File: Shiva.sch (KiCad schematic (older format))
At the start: 6 parts

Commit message: Add 8 input channels, Teensy, start MIDI interface
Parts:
- added BOARD?: BOARD_TEENSY_3.1, symbol BOARD_TEENSY_3.1
- added D? (x7): 3.3, symbol ZENER
- added D? (x7): 3.3V, symbol ZENER
- added D?: D, symbol D
- added J? (x7): JACK_FEMALE_STEREO, symbol CONNECTORS_JACK_FEMALE_STEREO_6_PINS
- added JP? (x8): Jumper_NO_Small, symbol Jumper_NO_Small
- added P? (x2): DIN_5, symbol DIN_5
- added R? (x7): 320M, symbol R
- added R? (x18): R, symbol R
- added U? (x8): LTC6242, symbol ANALOG_LTC6242
- D?: value ZENER -> 3.3
- D?: value ZENER -> 3.3V
- R?: value R -> 320M
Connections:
- net labels added: CHANNEL_01, CHANNEL_02, CHANNEL_03, CHANNEL_04, CHANNEL_05, CHANNEL_06, CHANNEL_07, CHANNEL_08, DETECT_02, DETECT_03, DETECT_04, DETECT_05, DETECT_06, DETECT_07, DETECT_08
- wire segments 18 -> 200
- no-connect marks 3 -> 24
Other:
- note added: "Features remaining:\n- MIDI OUT\n- MIDI IN ?\n- Regulator"
- moved on the sheet: D?, J?, R?

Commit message: Add MIDI and regulator
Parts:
- removed D?: D, symbol D
- removed P?: DIN_5, symbol DIN_5
- removed R? (x2): R, symbol R
- added C1, C2, C3: 100nF, symbol C
- added C4: 10uF, symbol C
- added JP10, JP9: Jumper_NO_Small, symbol Jumper_NO_Small
- added U3: LD1117S33CTR, SOT-223, symbol LD1117S33CTR
- R25, R26: renamed from R?; value R -> 220R
- gave numbers to parts that had none: 60
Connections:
- net CHANNEL_01: now also U1.16 (OUT); no longer U1.1 (OUT)
- net CHANNEL_04: now also U1.1 (OUT); no longer U1.16 (OUT)
- net CHANNEL_05: now also U2.16 (OUT); no longer U2.1 (OUT)
- net CHANNEL_06: now also U2.7 (OUT); no longer U2.1 (OUT)
- net CHANNEL_07: now also U2.10 (OUT); no longer U2.1 (OUT)
- net GND: now also BOARD1.1 (GND), P1.2; no longer U1.13 (V-), U1.13 (V-), U1.13 (V-), U1.13 (V-), U2.13 (V-), U2.13 (V-), U2.13 (V-), U2.13 (V-)
- net VCC: now also C1.1, C2.1, JP10.2, JP9.2
- net at D7.2 (A), D8.1 (K), J4.T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: now also U1.15 (-IN); no longer U1.2 (-IN)
- net at R12.2, R8.1: now also U1.14 (+IN); no longer U1.3 (+IN)
- net at D1.2 (A), D2.1 (K), J1.T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: now also U1.2 (-IN); no longer U1.15 (-IN)
- net at R5.1, R9.2: now also U1.3 (+IN); no longer U1.14 (+IN)
- net at D15.2 (A), D16.1 (K), J8.T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: now also U2.15 (-IN); no longer U2.2 (-IN)
- net at R20.1, R24.2: now also U2.14 (+IN); no longer U2.3 (+IN)
- net at D11.2 (A), D12.1 (K), J6.T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: now also U2.6 (-IN); no longer U2.2 (-IN)
- net at R18.1, R22.2: now also U2.5 (+IN); no longer U2.3 (+IN)
- net at D13.2 (A), D14.1 (K), J7.T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: now also U2.11 (-IN); no longer U2.2 (-IN)
- net at R19.1, R23.2: now also U2.12 (+IN); no longer U2.3 (+IN)
- net RX: now reaches BOARD1.2 (D0/RX1)
- net RX: now also R26.1
- net GNDA: now reaches BOARD1.27 (AGND)
- net GNDA: now also U1.13 (V-), U1.13 (V-), U1.13 (V-), U1.13 (V-), U2.13 (V-), U2.13 (V-), U2.13 (V-), U2.13 (V-), C1.2, C2.2, C3.2, C4.2, U3.1 (GND)
- net +5V: now reaches BOARD1.28 (Vin)
- net +5V: now also R25.1, C3.1, JP9.1, U3.3 (VI)
- net at P1.4: now also R26.2
- net at P1.5: now also R25.2
- new net: C4.1, JP10.1, U3.2 (VO)
- no-connect marks 24 -> 34
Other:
- note added: "(As close as possible \nto op-amp IC)"
- note added: "MIDI OUT"
- note added: "Select source at \nassembly"
- note removed: "Features remaining:\n- MIDI OUT\n- MIDI IN ?\n- Regulator"
- moved on the sheet: D1, D10, D11, D12, D13, D14, D15, D16, D2, D3, D4, D5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

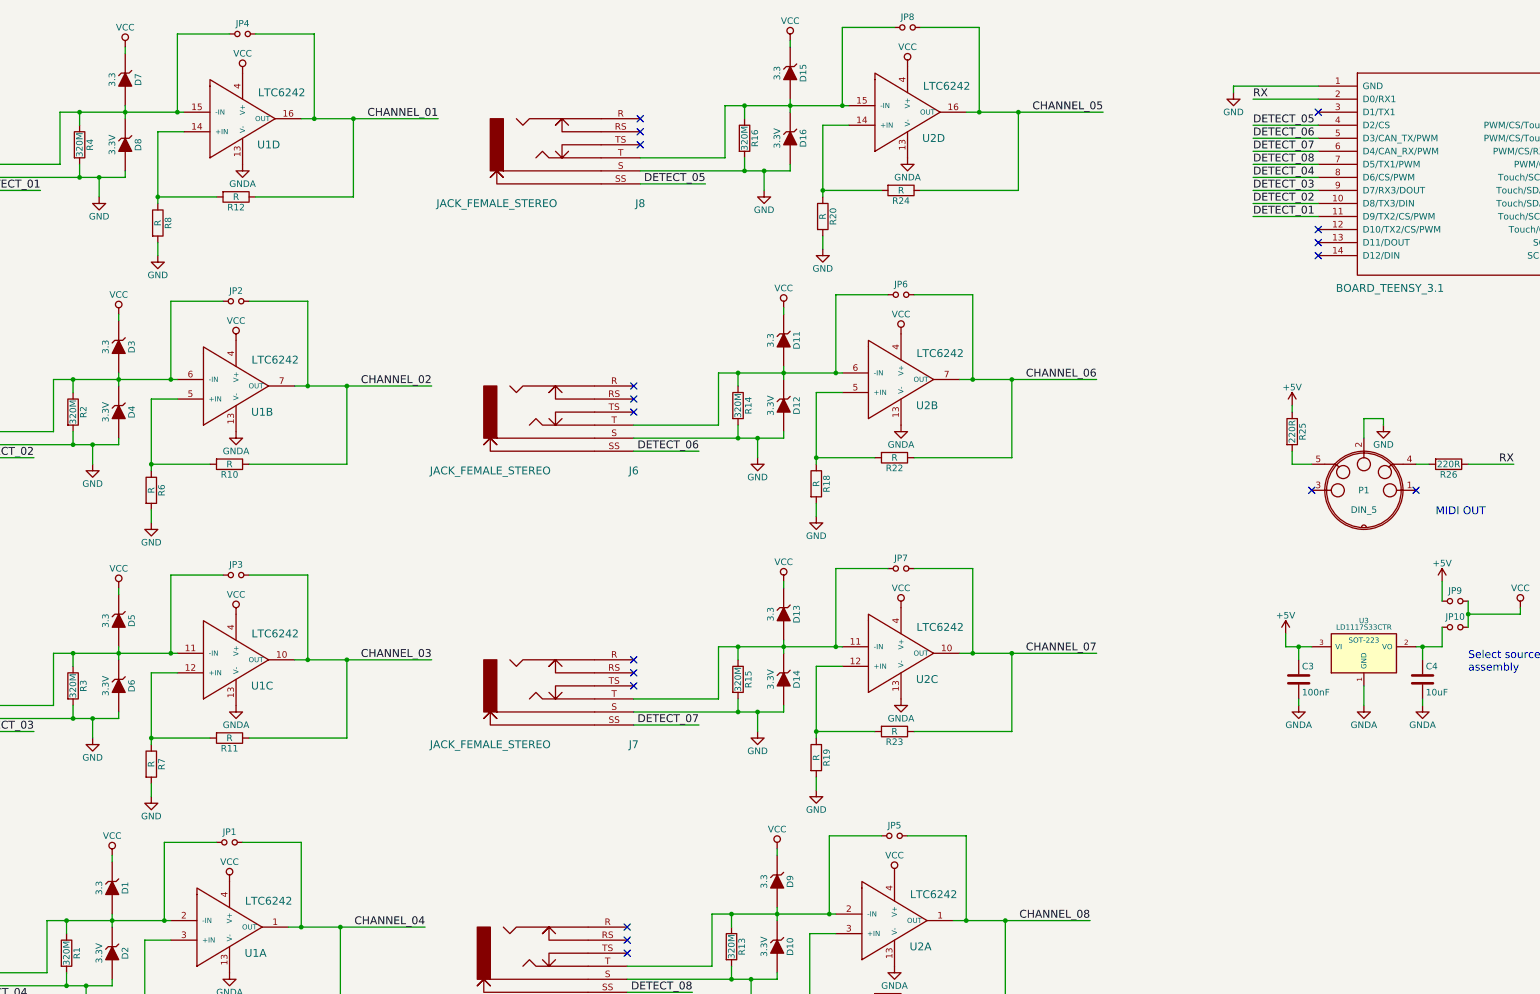
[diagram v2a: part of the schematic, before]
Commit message: Add some cmp assignments
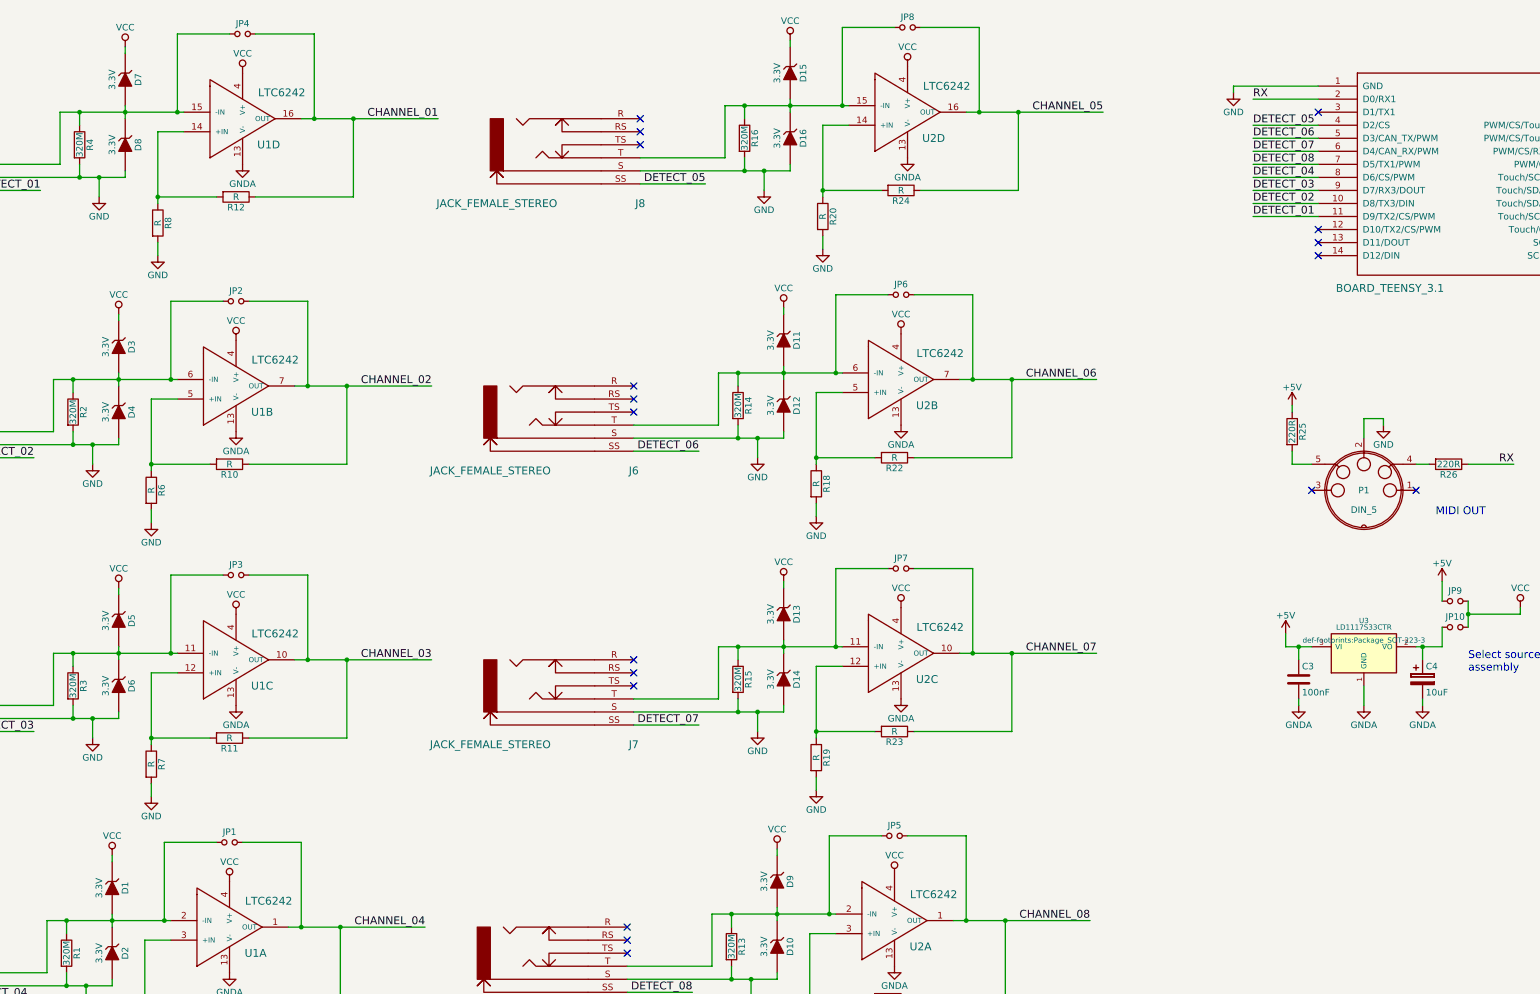
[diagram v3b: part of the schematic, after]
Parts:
- removed C4: 10uF, symbol C
- added C4: 10uF, symbol CP
- BOARD1: footprint (none) -> def-footprints:Board_Teensy_3_1
- C1, C2, C3: footprint (none) -> Capacitors_SMD:C_0805_HandSoldering
- D1, D11, D13, D15, D3, D5, D7, D9: value 3.3 -> 3.3V; footprint (none) -> Diodes_SMD:SOD-323
- D10, D12, D14, D16, D2, D4, D6, D8: footprint (none) -> Diodes_SMD:SOD-323
- J1, J2, J3, J4, J5, J6, J7, J8: footprint (none) -> def-footprints:CONN_Jack_Female_6.35mm_THD
- JP1, JP10, JP2, JP3, JP4, JP5, JP6, JP7, JP8, JP9: footprint (none) -> def-footprints:Miscellaneous_Solder_Jumper
- R1, R13, R14, R15, R16, R2, R3, R4, U1: footprint (none) -> Resistors_SMD:R_0805_HandSoldering
- R10, R11, R12, R17, R18, R19, R20, R21, R22, R23, R24, R25, R26, R5, R6, R7, R8, R9: footprint (none) -> Resistors_SMD:R_0603_HandSoldering
- U3: footprint SOT-223 -> def-footprints:Package_SOT-223-3
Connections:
- net GNDA: now also C4.2
- net at JP10.1, U3.2 (VO): now also C4.1

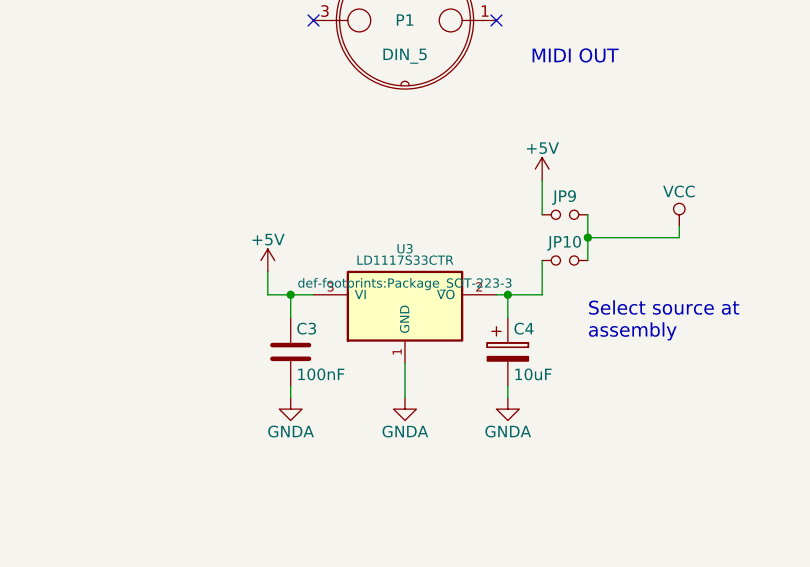
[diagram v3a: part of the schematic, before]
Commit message: Assign SSOP16 footprint
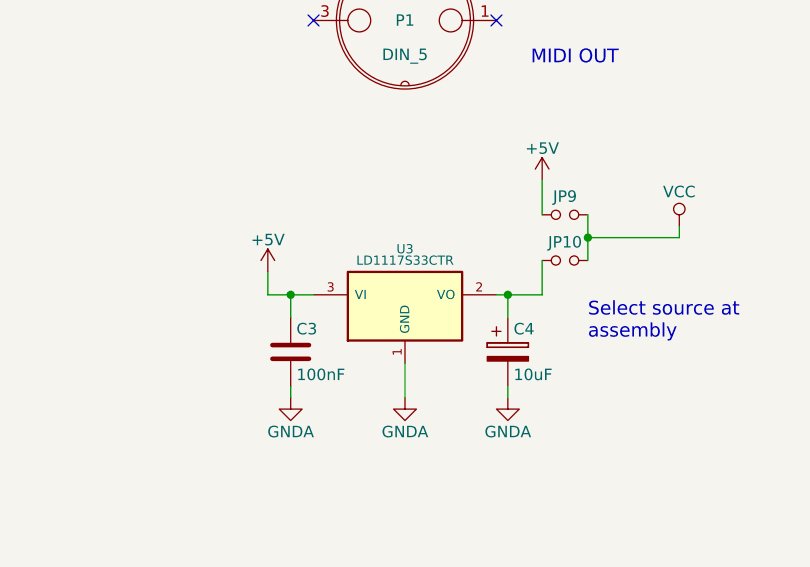
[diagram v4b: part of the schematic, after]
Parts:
- U1: footprint Resistors_SMD:R_0805_HandSoldering -> def-footprints:IC_SSOP16
- U2: footprint (none) -> def-footprints:IC_SSOP16
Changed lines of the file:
@@
 F 0 "U1" H 4500 1800 60  0000 C CNN
 F 1 "LTC6242" H 4600 2200 60  0000 C CNN
-F 2 "Resistors_SMD:R_0805_HandSoldering" H 4250 1850 60  0001 C CNN
+F 2 "def-footprints:IC_SSOP16" H 4250 1850 60  0001 C CNN
 F 3 "" H 4250 1850 60  0000 C CNN
 	4    4250 1850
@@
 F 0 "U1" H 4450 3850 60  0000 C CNN
 F 1 "LTC6242" H 4550 4250 60  0000 C CNN
-F 2 "Resistors_SMD:R_0805_HandSoldering" H 4200 3900 60  0001 C CNN
+F 2 "def-footprints:IC_SSOP16" H 4200 3900 60  0001 C CNN
 F 3 "" H 4200 3900 60  0000 C CNN
 	2    4200 3900
@@
 F 0 "U1" H 4450 5950 60  0000 C CNN
 F 1 "LTC6242" H 4550 6350 60  0000 C CNN
-F 2 "Resistors_SMD:R_0805_HandSoldering" H 4200 6000 60  0001 C CNN
+F 2 "def-footprints:IC_SSOP16" H 4200 6000 60  0001 C CNN
 F 3 "" H 4200 6000 60  0000 C CNN
 	3    4200 6000
@@
 F 0 "U1" H 4400 8000 60  0000 C CNN
 F 1 "LTC6242" H 4500 8400 60  0000 C CNN
-F 2 "Resistors_SMD:R_0805_HandSoldering" H 4150 8050 60  0001 C CNN
+F 2 "def-footprints:IC_SSOP16" H 4150 8050 60  0001 C CNN
 F 3 "" H 4150 8050 60  0000 C CNN
 	1    4150 8050
@@
 F 0 "U2" H 9600 1750 60  0000 C CNN
 F 1 "LTC6242" H 9700 2150 60  0000 C CNN
-F 2 "" H 9350 1800 60  0001 C CNN
+F 2 "def-footprints:IC_SSOP16" H 9350 1800 60  0001 C CNN
 F 3 "" H 9350 1800 60  0000 C CNN
 	4    9350 1800
@@
 F 0 "U2" H 9550 3800 60  0000 C CNN
 F 1 "LTC6242" H 9650 4200 60  0000 C CNN
-F 2 "" H 9300 3850 60  0001 C CNN
+F 2 "def-footprints:IC_SSOP16" H 9300 3850 60  0001 C CNN
 F 3 "" H 9300 3850 60  0000 C CNN
 	2    9300 3850
@@
 F 0 "U2" H 9550 5900 60  0000 C CNN
 F 1 "LTC6242" H 9650 6300 60  0000 C CNN
-F 2 "" H 9300 5950 60  0001 C CNN
+F 2 "def-footprints:IC_SSOP16" H 9300 5950 60  0001 C CNN
 F 3 "" H 9300 5950 60  0000 C CNN
 	3    9300 5950
@@
 F 0 "U2" H 9500 7950 60  0000 C CNN
 F 1 "LTC6242" H 9600 8350 60  0000 C CNN
-F 2 "" H 9250 8000 60  0001 C CNN
+F 2 "def-footprints:IC_SSOP16" H 9250 8000 60  0001 C CNN
 F 3 "" H 9250 8000 60  0000 C CNN
 	1    9250 8000
@@
 F 0 "U3" H 12900 6050 40  0000 C CNN
 F 1 "LD1117S33CTR" H 12900 6000 40  0000 C CNN
-F 2 "def-footprints:Package_SOT-223-3" H 12900 5900 40  0000 C CNN
+F 2 "def-footprints:Package_SOT-223-3" H 12900 5900 40  0001 C CNN
 F 3 "" H 12900 5800 60  0000 C CNN
 	1    12900 5800

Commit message: Assign 1206 pol to footprints
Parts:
- C4: footprint (none) -> def-footprints:Package_1206_pol
- U1, U2: footprint def-footprints:IC_SSOP16 -> def-footprints:Package_SSOP16
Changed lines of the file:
@@
 F 0 "U1" H 4500 1800 60  0000 C CNN
 F 1 "LTC6242" H 4600 2200 60  0000 C CNN
-F 2 "def-footprints:IC_SSOP16" H 4250 1850 60  0001 C CNN
+F 2 "def-footprints:Package_SSOP16" H 4250 1850 60  0001 C CNN
 F 3 "" H 4250 1850 60  0000 C CNN
 	4    4250 1850
@@
 F 0 "U1" H 4450 3850 60  0000 C CNN
 F 1 "LTC6242" H 4550 4250 60  0000 C CNN
-F 2 "def-footprints:IC_SSOP16" H 4200 3900 60  0001 C CNN
+F 2 "def-footprints:Package_SSOP16" H 4200 3900 60  0001 C CNN
 F 3 "" H 4200 3900 60  0000 C CNN
 	2    4200 3900
@@
 F 0 "U1" H 4450 5950 60  0000 C CNN
 F 1 "LTC6242" H 4550 6350 60  0000 C CNN
-F 2 "def-footprints:IC_SSOP16" H 4200 6000 60  0001 C CNN
+F 2 "def-footprints:Package_SSOP16" H 4200 6000 60  0001 C CNN
 F 3 "" H 4200 6000 60  0000 C CNN
 	3    4200 6000
@@
 F 0 "U1" H 4400 8000 60  0000 C CNN
 F 1 "LTC6242" H 4500 8400 60  0000 C CNN
-F 2 "def-footprints:IC_SSOP16" H 4150 8050 60  0001 C CNN
+F 2 "def-footprints:Package_SSOP16" H 4150 8050 60  0001 C CNN
 F 3 "" H 4150 8050 60  0000 C CNN
 	1    4150 8050
@@
 F 0 "U2" H 9600 1750 60  0000 C CNN
 F 1 "LTC6242" H 9700 2150 60  0000 C CNN
-F 2 "def-footprints:IC_SSOP16" H 9350 1800 60  0001 C CNN
+F 2 "def-footprints:Package_SSOP16" H 9350 1800 60  0001 C CNN
 F 3 "" H 9350 1800 60  0000 C CNN
 	4    9350 1800
@@
 F 0 "U2" H 9550 3800 60  0000 C CNN
 F 1 "LTC6242" H 9650 4200 60  0000 C CNN
-F 2 "def-footprints:IC_SSOP16" H 9300 3850 60  0001 C CNN
+F 2 "def-footprints:Package_SSOP16" H 9300 3850 60  0001 C CNN
 F 3 "" H 9300 3850 60  0000 C CNN
 	2    9300 3850
@@
 F 0 "U2" H 9550 5900 60  0000 C CNN
 F 1 "LTC6242" H 9650 6300 60  0000 C CNN
-F 2 "def-footprints:IC_SSOP16" H 9300 5950 60  0001 C CNN
+F 2 "def-footprints:Package_SSOP16" H 9300 5950 60  0001 C CNN
 F 3 "" H 9300 5950 60  0000 C CNN
 	3    9300 5950
@@
 F 0 "U2" H 9500 7950 60  0000 C CNN
 F 1 "LTC6242" H 9600 8350 60  0000 C CNN
-F 2 "def-footprints:IC_SSOP16" H 9250 8000 60  0001 C CNN
+F 2 "def-footprints:Package_SSOP16" H 9250 8000 60  0001 C CNN
 F 3 "" H 9250 8000 60  0000 C CNN
 	1    9250 8000
@@
 F 0 "C4" H 13375 6100 50  0000 L CNN
 F 1 "10uF" H 13375 5900 50  0000 L CNN
-F 2 "" H 13388 5850 30  0001 C CNN
+F 2 "def-footprints:Package_1206_pol" H 13388 5850 30  0001 C CNN
 F 3 "" H 13350 6000 60  0000 C CNN
 	1    13350 6000

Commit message: Preliminary routing
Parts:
- P1: footprint (none) -> def-footprints:CONN_DIN5_Socket
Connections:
- net GNDA is gone; now on net GND: BOARD1.27 (AGND), C1.2, C2.2, C3.2, C4.2, U1.13 (V-), U1.13 (V-), U1.13 (V-), U1.13 (V-), U2.13 (V-), U2.13 (V-), U2.13 (V-), U2.13 (V-), U3.1 (GND)
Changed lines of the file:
@@
 F 0 "P1" H 12900 4550 50  0000 C CNN
 F 1 "DIN_5" H 12900 4400 50  0000 C CNN
-F 2 "" H 12900 4550 60  0001 C CNN
+F 2 "def-footprints:CONN_DIN5_Socket" H 12900 4550 60  0001 C CNN
 F 3 "" H 12900 4550 60  0000 C CNN
 	1    12900 4550
@@
 	1    0    0    -1
 $EndComp
+Wire Wire Line
+	15400 6600 15600 6600
+Connection ~ 15600 6600
+Connection ~ 15400 6600
 $EndSCHEMATC

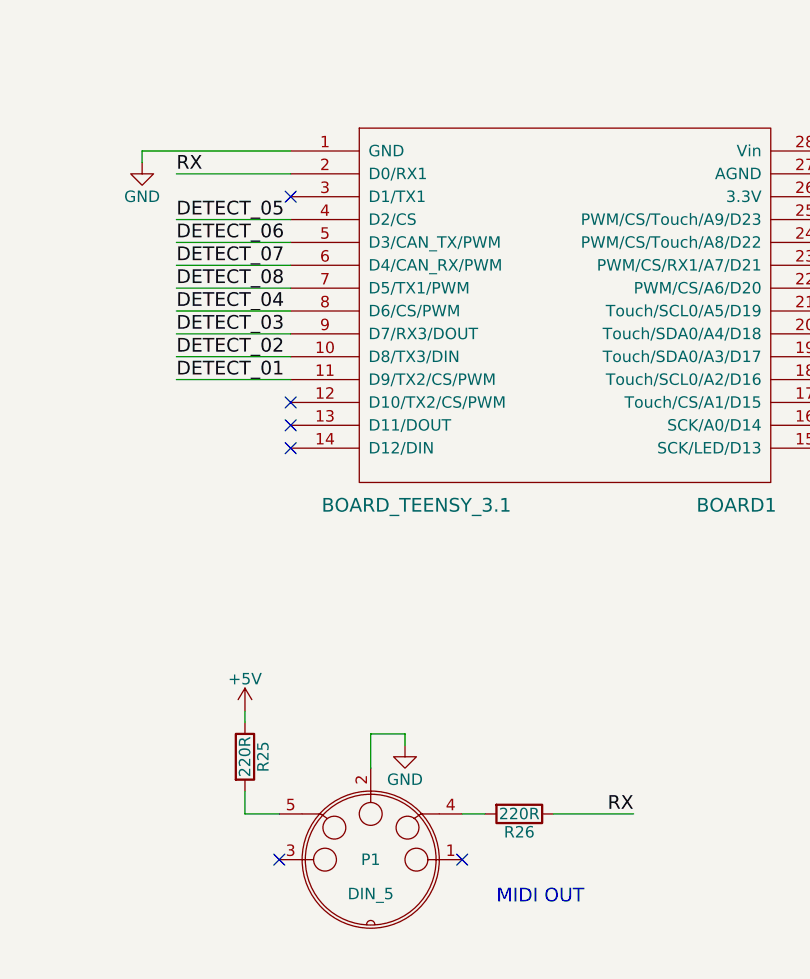
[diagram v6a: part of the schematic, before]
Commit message: Fix bug with midi tx. Finish silkscreen
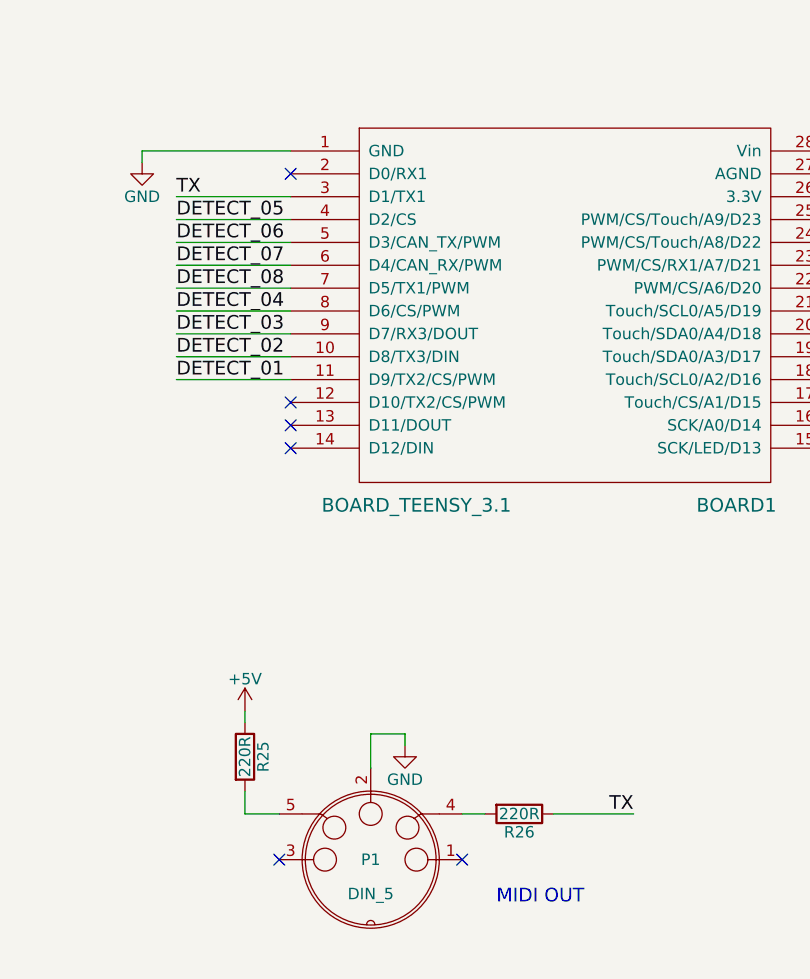
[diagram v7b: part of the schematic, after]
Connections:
- net TX: now reaches BOARD1.3 (D1/TX1)
- net TX: now also R26.1
- net RX: no longer names the net of BOARD1.2 (D0/RX1)
- net RX: no longer R26.1
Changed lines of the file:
@@
 	13700 4350 14050 4350
 Text Label 14050 4350 2    60   ~ 0
-RX
-Text Label 12050 1550 0    60   ~ 0
-RX
-Wire Wire Line
-	12050 1550 12550 1550
+TX
+Text Label 12050 1650 0    60   ~ 0
+TX
+Wire Wire Line
+	12050 1650 12550 1650
 Wire Wire Line
 	14950 1450 15050 1450
@@
 Wire Wire Line
 	11900 1450 12550 1450
-NoConn ~ 12550 1650
 NoConn ~ 12550 2550
 NoConn ~ 12550 2650
@@
 Connection ~ 15600 6600
 Connection ~ 15400 6600
+NoConn ~ 12550 1550
 $EndSCHEMATC
